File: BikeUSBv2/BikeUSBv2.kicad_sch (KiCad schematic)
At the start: 33 parts, among them J1 USB_C_Receptacle_PowerOnly_6P, Q1 Q_PMOS_GSD, SW1 SW_DPST, U1 TPS63020DSJR

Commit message: todia
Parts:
- D1: value LED -> red
- D2: value LED -> blue
- D3: value LED -> green
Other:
- note added: "IDEA: CR filter for detecting high generator RPM and switching on 1.5A mode resistors"
- note added: "TODO: cool looking power conversion steps graphics for pcb"
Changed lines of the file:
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@@
     (stroke (width 0) (type default))
+  )
+  (text "TODO: cool looking power conversion steps graphics for pcb"
+    (at 50.165 135.89 0)
+    (effects (font (size 1.27 1.27)) (justify left bottom))
+  )
+  (text "IDEA: CR filter for detecting high generator RPM and switching on 1.5A mode resistors"
+    (at 43.18 146.685 0)
+    (effects (font (size 1.27 1.27)) (justify left bottom))
   )
   (label "AC2" (at 43.18 88.265 180) (fields_autoplaced)
@@
       (effects (font (size 1.27 1.27)) (justify right))
     )
-    (property "Value" "LED" (at 142.875 130.175 90)
+    (property "Value" "green" (at 142.875 130.175 90)
       (effects (font (size 1.27 1.27)) (justify right))
     )
@@
   (symbol (lib_id "Device:LED") (at 124.46 127.635 90) (unit 1)
     (in_bom yes) (on_board yes) (dnp no) (fields_autoplaced)
-    (property "Reference" "D2" (at 127.635 127.9525 90)
+    (property "Reference" "D2" (at 128.27 127.9525 90)
       (effects (font (size 1.27 1.27)) (justify right))
     )
-    (property "Value" "LED" (at 127.635 130.4925 90)
+    (property "Value" "blue" (at 128.27 130.4925 90)
       (effects (font (size 1.27 1.27)) (justify right))
     )
@@
   (symbol (lib_id "Device:LED") (at 26.67 129.54 90) (unit 1)
     (in_bom yes) (on_board yes) (dnp no) (fields_autoplaced)
-    (property "Reference" "D1" (at 29.845 129.8575 90)
+    (property "Reference" "D1" (at 30.48 129.8575 90)
       (effects (font (size 1.27 1.27)) (justify right))
     )
-    (property "Value" "LED" (at 29.845 132.3975 90)
+    (property "Value" "red" (at 30.48 132.3975 90)
       (effects (font (size 1.27 1.27)) (justify right))
     )

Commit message: some things
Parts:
- C1: value 22u -> 100n
- C2: value 22u -> 10u
- C7: value 10u -> 22u
- D4, D5, D6, D7: value D -> CMS04(TE12L,Q,M); footprint (none) -> Diode_SMD:D_SOD-128; symbol Device:D -> Device:D_Schottky
- D8: value 5V5 -> 1SMB5919BT3G; footprint (none) -> Diode_SMD:D_SMB-SMC_Universal_Handsoldering; LCSC Part (none) -> C7422622
- J1: value USB_C_Receptacle_PowerOnly_6P -> TYPE-C-31-M-16
- JP1: footprint (none) -> Jumper:SolderJumper-2_P1.3mm_Bridged_RoundedPad1.0x1.5mm
- Q1: value Q_PMOS_GSD -> SSM3J332R,LF
- R10: value R -> 47k
- R9: value R -> 4k7
- SW1: value SW_DPST -> 5.8 ZSPT
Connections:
- net VCC: no longer C1.1, U1.1 (VINA), U1.12 (EN)
- new net: C1.1, U1.1 (VINA)
- new net EN: U1.12 (EN)
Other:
- note added: "IDEA: voltage threshold for 1.5A Mode"
- moved on the sheet: C9, D8, JP1

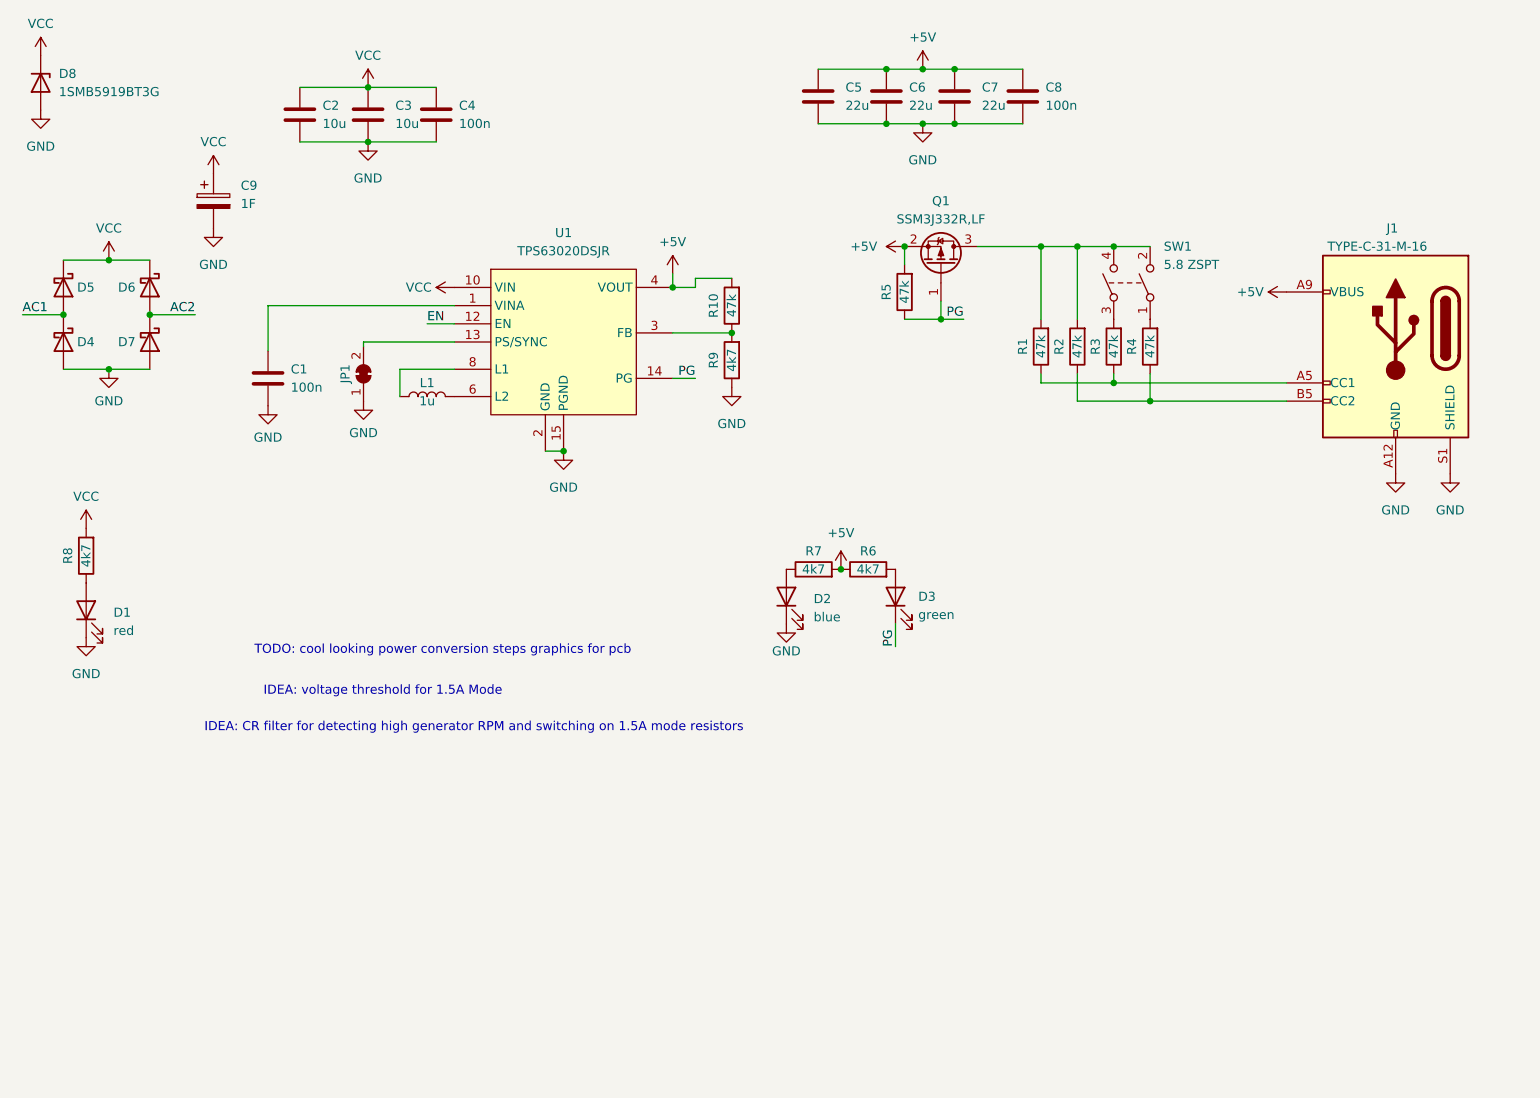
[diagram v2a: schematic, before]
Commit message: fine, im using an MCU
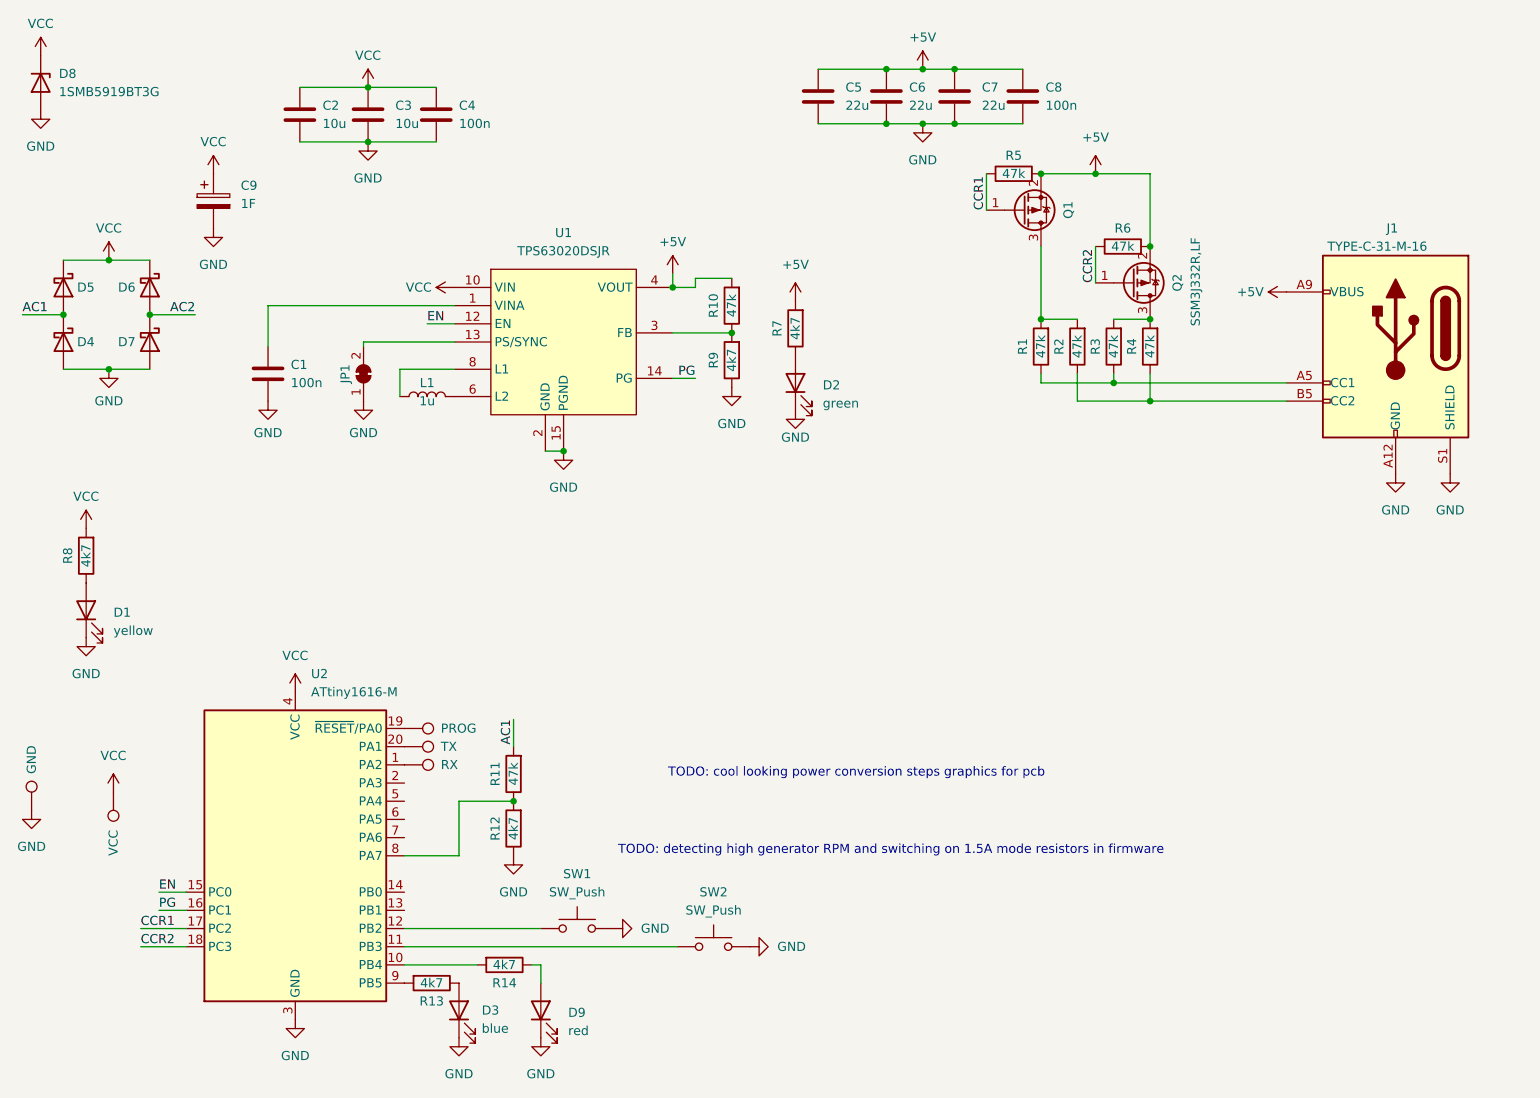
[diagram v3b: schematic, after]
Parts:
- removed SW1: 5.8 ZSPT, symbol Switch:SW_DPST
- added D9: red, LED_SMD:LED_0805_2012Metric_Pad1.15x1.40mm_HandSolder, symbol Device:LED
- added Q2: SSM3J332R,LF, Package_TO_SOT_SMD:SOT-23_Handsoldering, symbol Device:Q_PMOS_GSD
- added R11: 47k, Resistor_SMD:R_0805_2012Metric_Pad1.20x1.40mm_HandSolder, symbol Device:R
- added R12, R13, R14: 4k7, Resistor_SMD:R_0805_2012Metric_Pad1.20x1.40mm_HandSolder, symbol Device:R
- added SW1, SW2: SW_Push, symbol Switch:SW_Push
- added TP1: PROG, symbol Connector:TestPoint
- added TP2: GND, symbol Connector:TestPoint
- added TP3: VCC, symbol Connector:TestPoint
- added TP4: TX, symbol Connector:TestPoint
- added TP5: RX, symbol Connector:TestPoint
- added U2: ATtiny1616-M, Package_DFN_QFN:VQFN-20-1EP_3x3mm_P0.4mm_EP1.7x1.7mm, symbol MCU_Microchip_ATtiny:ATtiny1616-M
- C9: footprint (none) -> Capacitor_THT:CP_Radial_D8.0mm_P5.00mm
- D1: value red -> yellow; footprint (none) -> LED_SMD:LED_0805_2012Metric_Pad1.15x1.40mm_HandSolder
- D2: value blue -> green; footprint (none) -> LED_SMD:LED_0805_2012Metric_Pad1.15x1.40mm_HandSolder
- D3: value green -> blue; footprint (none) -> LED_SMD:LED_0805_2012Metric_Pad1.15x1.40mm_HandSolder
- J1: footprint (none) -> easyeda2kicad:TYPE-C-SMD_TYPE-C-31-M-16
- L1: footprint (none) -> Capacitor_SMD:C_0805_2012Metric_Pad1.18x1.45mm_HandSolder
- Q1: footprint (none) -> Package_TO_SOT_SMD:SOT-23_Handsoldering
- R6: value 4k7 -> 47k
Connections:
- net +5V: now also R6.2, Q2.2 (S); no longer R6.1
- net AC1: now also R11.2
- net EN: now also U2.15 (PC0)
- net GND: now also D3.1 (K), D9.1 (K), R12.1, SW1.2, SW2.2, TP2.1, U2.21 (GND), U2.3 (GND)
- net PG: now also U2.16 (PC1); no longer D3.1 (K), Q1.1 (G), R5.1
- net VCC: now also TP3.1, U2.4 (VCC)
- net at R4.2: now also R3.2, Q2.3 (D)
- net at D3.2 (A): now also R13.1; no longer R6.2
- new net: D9.2 (A), R14.1
- new net: R14.2, U2.10 (PB4)
- new net: SW2.1, U2.11 (PB3)
- new net: TP4.1, U2.20 (PA1)
- new net: R11.1, R12.2, U2.8 (PA7)
- new net: R13.2, U2.9 (PB5)
- new net: SW1.1, U2.12 (PB2)
- new net: TP5.1, U2.1 (PA2)
- new net: TP1.1, U2.19 (~{RESET}/PA0)
- new net CCR1: Q1.1 (G), R5.1, U2.17 (PC2)
- new net CCR2: Q2.1 (G), R6.1, U2.18 (PC3)
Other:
- note added: "TODO: detecting high generator RPM and switching on 1.5A mode resistors in firmware"
- note removed: "IDEA: CR filter for detecting high generator RPM and switching on 1.5A mode resistors"
- note removed: "IDEA: voltage threshold for 1.5A Mode"
- moved on the sheet: C1, D2, Q1, R7

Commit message: group things on PCB
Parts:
- L1: footprint Capacitor_SMD:C_0805_2012Metric_Pad1.18x1.45mm_HandSolder -> Inductor_SMD:L_7.3x7.3_H4.5
- SW1, SW2: footprint (none) -> Button_Switch_SMD:SW_SPST_CK_RS282G05A3
- TP1, TP2, TP3, TP4, TP5: footprint (none) -> TestPoint:TestPoint_Pad_D2.5mm
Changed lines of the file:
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@@
       (effects (font (size 1.27 1.27)) (justify right))
     )
-    (property "Footprint" "" (at 25.4 154.94 0)
+    (property "Footprint" "TestPoint:TestPoint_Pad_D2.5mm" (at 25.4 154.94 0)
       (effects (font (size 1.27 1.27)) hide)
     )
@@
       (effects (font (size 1.27 1.27)))
     )
-    (property "Footprint" "" (at 114.3 171.45 0)
+    (property "Footprint" "Button_Switch_SMD:SW_SPST_CK_RS282G05A3" (at 114.3 171.45 0)
       (effects (font (size 1.27 1.27)) hide)
     )
@@
       (effects (font (size 1.27 1.27)) (justify left))
     )
-    (property "Footprint" "" (at 24.13 157.48 0)
+    (property "Footprint" "TestPoint:TestPoint_Pad_D2.5mm" (at 24.13 157.48 0)
       (effects (font (size 1.27 1.27)) hide)
     )
@@
       (effects (font (size 1.27 1.27)) (justify left))
     )
-    (property "Footprint" "" (at 71.12 153.67 0)
+    (property "Footprint" "TestPoint:TestPoint_Pad_D2.5mm" (at 71.12 153.67 0)
       (effects (font (size 1.27 1.27)) hide)
     )
@@
       (effects (font (size 1.27 1.27)))
     )
-    (property "Footprint" "Capacitor_SMD:C_0805_2012Metric_Pad1.18x1.45mm_HandSolder" (at 74.295 99.695 0)
+    (property "Footprint" "Inductor_SMD:L_7.3x7.3_H4.5" (at 74.295 99.695 0)
       (effects (font (size 1.27 1.27)) hide)
     )
@@
       (effects (font (size 1.27 1.27)))
     )
-    (property "Footprint" "" (at 95.25 168.91 0)
+    (property "Footprint" "Button_Switch_SMD:SW_SPST_CK_RS282G05A3" (at 95.25 168.91 0)
       (effects (font (size 1.27 1.27)) hide)
     )
@@
       (effects (font (size 1.27 1.27)) (justify left))
     )
-    (property "Footprint" "" (at 71.12 156.21 0)
+    (property "Footprint" "TestPoint:TestPoint_Pad_D2.5mm" (at 71.12 156.21 0)
       (effects (font (size 1.27 1.27)) hide)
     )
@@
       (effects (font (size 1.27 1.27)) (justify left))
     )
-    (property "Footprint" "" (at 71.12 151.13 0)
-      (effects (font (size 1.27 1.27)) hide)
-    )
+    (property "Footprint" "TestPoint:TestPoint_Pad_D2.5mm" (at 71.12 151.13 0)
+      (effects (font (size 1.27 1.27)) hide)
+    )

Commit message: dont exactly remember what i did here, its from tuesday i think
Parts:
- added J2: Conn_01x02_Female, Connector_JST:JST_EH_S2B-EH_1x02_P2.50mm_Horizontal, symbol Connector:Conn_01x02_Female
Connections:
- net AC1: now also J2.2 (Pin_2)
- net AC2: now also J2.1 (Pin_1)
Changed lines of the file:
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@@
     (effects (font (size 1.27 1.27)) (justify left bottom))
+  )
+  (label "AC2" (at 33.02 106.68 180) (fields_autoplaced)
+    (effects (font (size 1.27 1.27)) (justify right bottom))
   )
   (label "AC2" (at 41.91 88.265 180) (fields_autoplaced)
@@
   (label "CCR2" (at 34.29 176.53 0) (fields_autoplaced)
     (effects (font (size 1.27 1.27)) (justify left bottom))
+  )
+  (label "AC1" (at 33.02 109.22 180) (fields_autoplaced)
+    (effects (font (size 1.27 1.27)) (justify right bottom))
   )
   (symbol (lib_id "Device:R") (at 156.21 68.58 90) (unit 1)
@@
         )
       )
+    )
+  )
+  (symbol (lib_id "Connector:Conn_01x02_Female") (at 38.1 106.68 0) (unit 1)
+    (in_bom yes) (on_board yes) (dnp no) (fields_autoplaced)
+    (property "Reference" "J2" (at 39.37 106.68 0)
+      (effects (font (size 1.27 1.27)) (justify left))
+    )
+    (property "Value" "Conn_01x02_Female" (at 39.37 109.22 0)
+      (effects (font (size 1.27 1.27)) (justify left))
+    )
+    (property "Footprint" "Connector_JST:JST_EH_S2B-EH_1x02_P2.50mm_Horizontal" (at 38.1 106.68 0)
+      (effects (font (size 1.27 1.27)) hide)
+    )
+    (property "Datasheet" "~" (at 38.1 106.68 0)
+      (effects (font (size 1.27 1.27)) hide)
+    )
+    (pin "1")
+    (pin "2")
+    (instances
+      (project "BikeUSBv2"
+        (path "/b4aff538-5116-4944-9d24-c26a88d7dfe8"
+          (reference "J2") (unit 1)
+        )
+      )

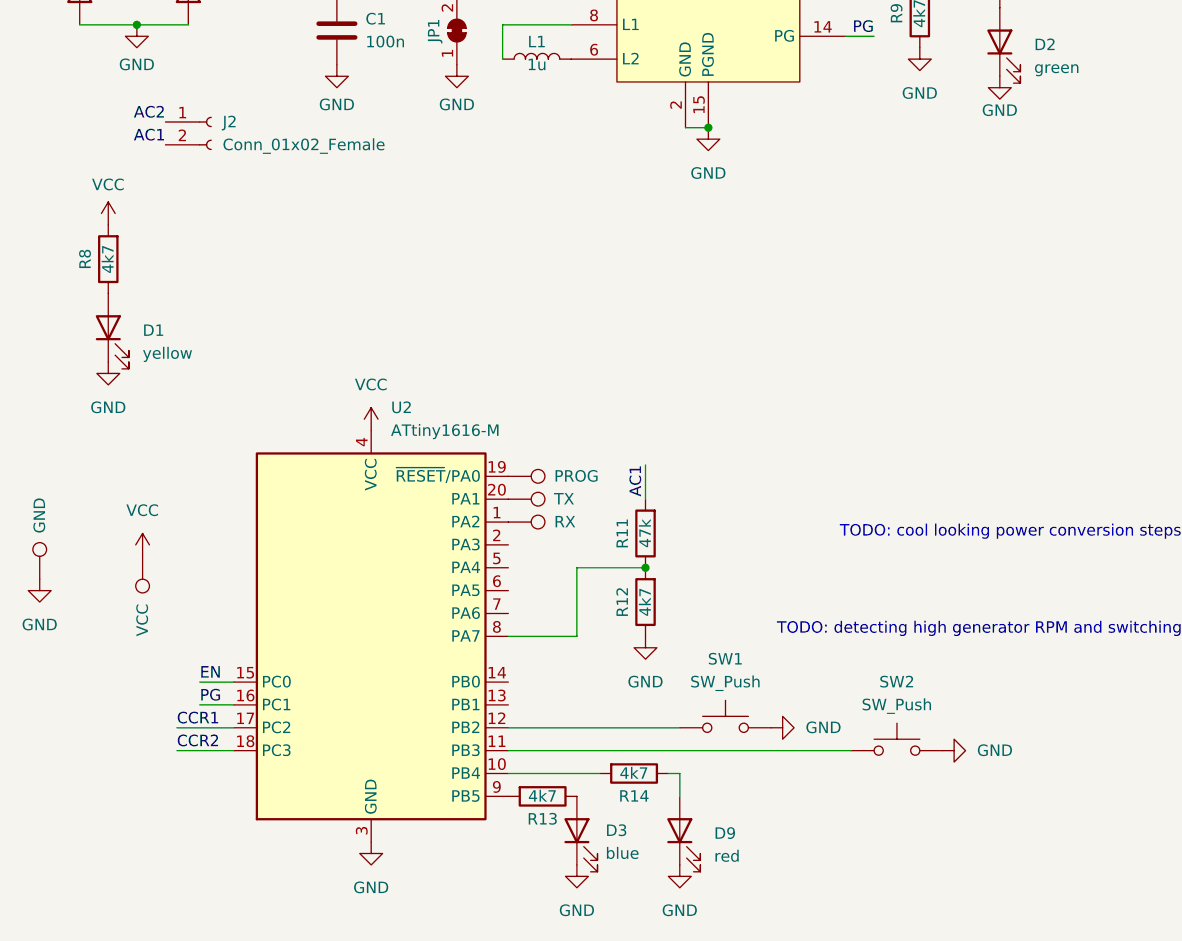
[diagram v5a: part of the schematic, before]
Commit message: placed components, started routing
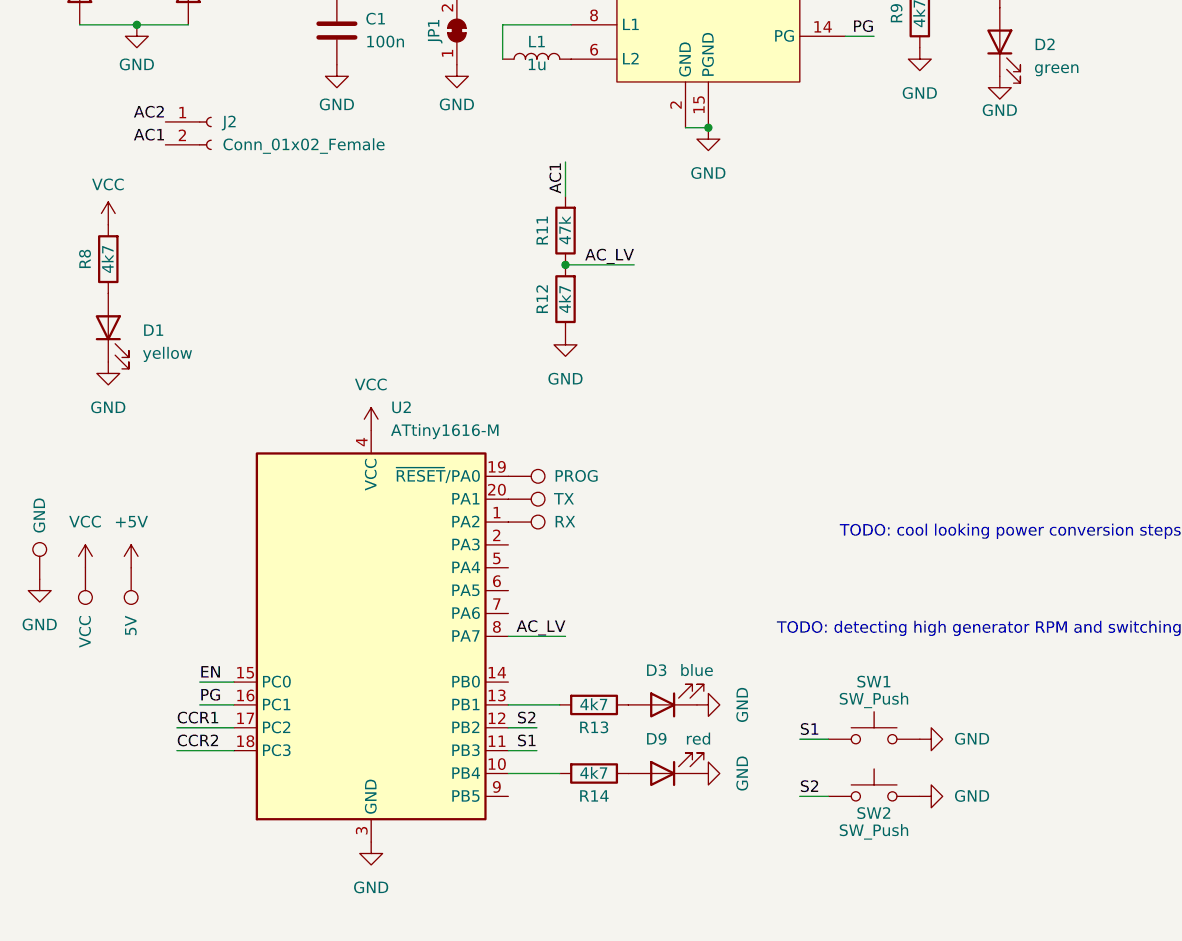
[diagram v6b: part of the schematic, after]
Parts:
- added TP6: 5V, TestPoint:TestPoint_Pad_D2.5mm, symbol Connector:TestPoint
- C5, C6, C7: footprint Capacitor_SMD:C_0805_2012Metric_Pad1.18x1.45mm_HandSolder -> Capacitor_SMD:C_1206_3216Metric_Pad1.33x1.80mm_HandSolder
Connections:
- net +5V: now also TP6.1
- net S1: now reaches U2.11 (PB3)
- net S1: now also SW1.1; no longer SW2.1
- net  AC_LV: now reaches R11.1, R12.2, U2.8 (PA7)
- net at R13.2: now also U2.13 (PB1); no longer U2.9 (PB5)
- net S2: now reaches U2.12 (PB2)
- net S2: now also SW2.1; no longer SW1.1
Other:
- moved on the sheet: D3, D9, R11, R12, R13, R14, SW1, SW2

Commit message: routing finished so far
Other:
- note added: "TODO: check if button pins are interrupt capable"
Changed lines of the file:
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@@
+    (effects (font (size 1.27 1.27)) (justify left bottom))
+  )
+  (text "TODO: check if button pins are interrupt capable" (at 80.645 158.115 0)
     (effects (font (size 1.27 1.27)) (justify left bottom))
   )
